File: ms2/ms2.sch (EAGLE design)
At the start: 127 parts, among them J1 POWERPOLE_POWER25A, J10 RS485_1, J11 I2C, J12 TTL_SERIAL, J13 Radio, J14 RS485_3, J2 RAIN, J3 ADC1, J4 ON, J5 D1, J6 D2, J7 ADC2, J8 LED-EN, J9 RS485_2, Q1 DMG6602SVT, Q2 DMG6602SVT, Q3 DMG6602SVT, Q4 DMG6602SVT, U1 LT1934ES6TRMPBF, U2 LT1934ES6TRMPBF, U3 DS3231SN, U4 ISL3179EIBZ, U5 ISL3179EIBZ, U6 ISL3179EIBZ, X1 KUSBVX-BS1N

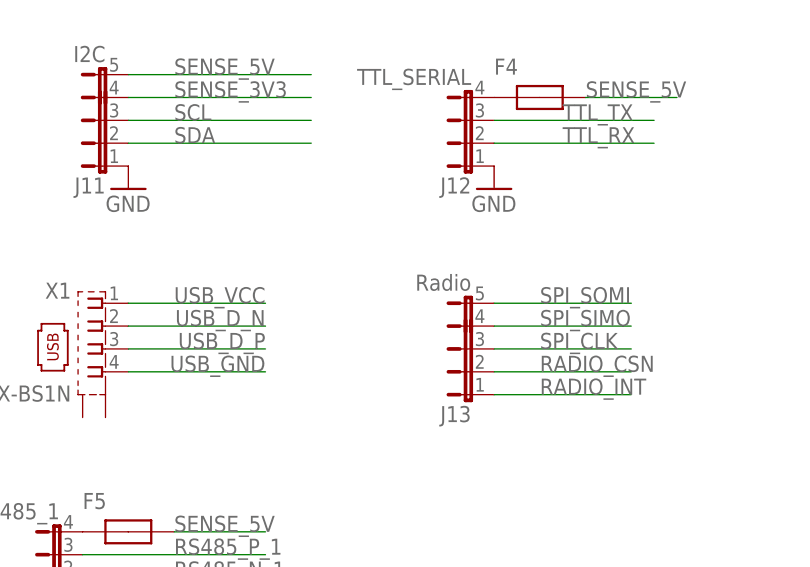
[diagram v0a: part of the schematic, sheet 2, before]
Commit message: CC1120 rotated
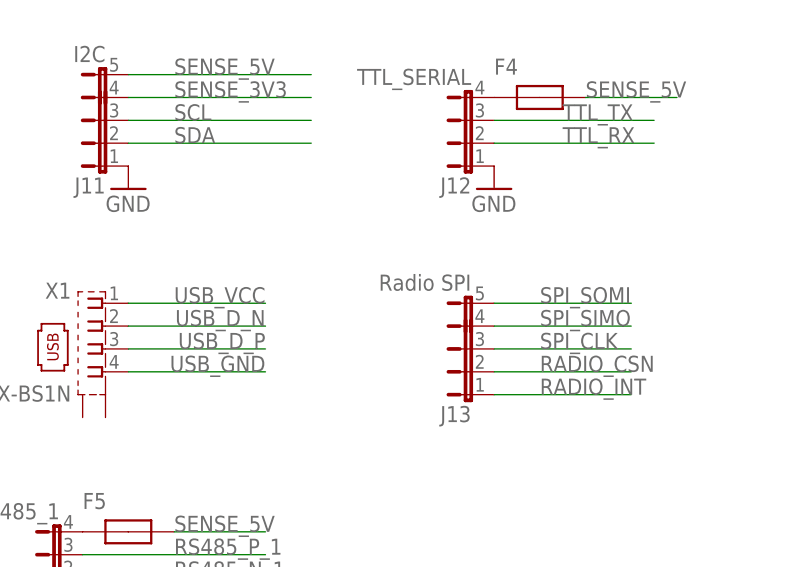
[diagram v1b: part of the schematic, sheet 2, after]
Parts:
- J13: value Radio -> Radio SPI
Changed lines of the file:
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@@
 <?xml version="1.0" encoding="utf-8"?>
 <!DOCTYPE eagle SYSTEM "eagle.dtd">
-<eagle version="6.4">
+<eagle version="6.5.0">
 <drawing>
 <settings>
@@
 <part name="GND10" library="glacsweb" deviceset="GND" device=""/>
 <part name="JP3" library="SparkFun-Passives" deviceset="JUMPER-2" device="SMD-NC"/>
-<part name="J13" library="farnell-parts" deviceset="5-PIN-MOLEX" device="" value="Radio"/>
+<part name="J13" library="farnell-parts" deviceset="5-PIN-MOLEX" device="" value="Radio SPI"/>
 <part name="R16" library="resistor" deviceset="R-EU_" device="R0805" value="56"/>
 <part name="LED3" library="led" deviceset="LED" device="CHIP-LED0805" value="RAIN"/>

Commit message: Work on MS2
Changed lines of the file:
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@@
 <?xml version="1.0" encoding="utf-8"?>
 <!DOCTYPE eagle SYSTEM "eagle.dtd">
-<eagle version="6.5.0">
+<eagle version="6.4">
 <drawing>
 <settings>
@@
 <net name="TXEN" class="0">
 <segment>
+<pinref part="U$5" gate="G$1" pin="CA0"/>
+<wire x1="38.1" y1="177.8" x2="20.32" y2="177.8" width="0.1524" layer="91"/>
+<label x="20.32" y="177.8" size="1.778" layer="95"/>
+</segment>
+<segment>
+<pinref part="U6" gate="A" pin="~RE"/>
+<wire x1="172.72" y1="76.2" x2="170.18" y2="76.2" width="0.1524" layer="91"/>
+<label x="160.02" y="76.2" size="1.778" layer="95"/>
+<pinref part="U6" gate="A" pin="DE"/>
+<wire x1="170.18" y1="76.2" x2="160.02" y2="76.2" width="0.1524" layer="91"/>
+<wire x1="172.72" y1="73.66" x2="170.18" y2="73.66" width="0.1524" layer="91"/>
+<wire x1="170.18" y1="73.66" x2="170.18" y2="76.2" width="0.1524" layer="91"/>
+<junction x="170.18" y="76.2"/>
+<pinref part="U5" gate="A" pin="~RE"/>
+<wire x1="175.26" y1="127" x2="172.72" y2="127" width="0.1524" layer="91"/>
+<label x="160.02" y="127" size="1.778" layer="95"/>
+<pinref part="U5" gate="A" pin="DE"/>
+<wire x1="172.72" y1="127" x2="160.02" y2="127" width="0.1524" layer="91"/>
+<wire x1="175.26" y1="124.46" x2="172.72" y2="124.46" width="0.1524" layer="91"/>
+<wire x1="172.72" y1="124.46" x2="172.72" y2="127" width="0.1524" layer="91"/>
+<junction x="172.72" y="127"/>
+<wire x1="160.02" y1="76.2" x2="160.02" y2="127" width="0.1524" layer="91"/>
 <pinref part="U4" gate="A" pin="~RE"/>
 <wire x1="175.26" y1="175.26" x2="172.72" y2="175.26" width="0.1524" layer="91"/>
@@
 <wire x1="172.72" y1="172.72" x2="172.72" y2="175.26" width="0.1524" layer="91"/>
 <junction x="172.72" y="175.26"/>
-</segment>
-<segment>
-<pinref part="U$5" gate="G$1" pin="CA0"/>
-<wire x1="38.1" y1="177.8" x2="20.32" y2="177.8" width="0.1524" layer="91"/>
-<label x="20.32" y="177.8" size="1.778" layer="95"/>
-</segment>
-<segment>
-<pinref part="U5" gate="A" pin="~RE"/>
-<wire x1="175.26" y1="127" x2="172.72" y2="127" width="0.1524" layer="91"/>
-<label x="160.02" y="127" size="1.778" layer="95"/>
-<pinref part="U5" gate="A" pin="DE"/>
-<wire x1="172.72" y1="127" x2="160.02" y2="127" width="0.1524" layer="91"/>
-<wire x1="175.26" y1="124.46" x2="172.72" y2="124.46" width="0.1524" layer="91"/>
-<wire x1="172.72" y1="124.46" x2="172.72" y2="127" width="0.1524" layer="91"/>
-<junction x="172.72" y="127"/>
-</segment>
-<segment>
-<pinref part="U6" gate="A" pin="~RE"/>
-<wire x1="172.72" y1="76.2" x2="170.18" y2="76.2" width="0.1524" layer="91"/>
-<label x="157.48" y="76.2" size="1.778" layer="95"/>
-<pinref part="U6" gate="A" pin="DE"/>
-<wire x1="170.18" y1="76.2" x2="157.48" y2="76.2" width="0.1524" layer="91"/>
-<wire x1="172.72" y1="73.66" x2="170.18" y2="73.66" width="0.1524" layer="91"/>
-<wire x1="170.18" y1="73.66" x2="170.18" y2="76.2" width="0.1524" layer="91"/>
-<junction x="170.18" y="76.2"/>
-</segment>
-</net>
+<wire x1="160.02" y1="127" x2="160.02" y2="175.26" width="0.1524" layer="91"/>
+<wire x1="160.02" y1="175.26" x2="160.02" y2="198.12" width="0.1524" layer="91"/>
+<wire x1="160.02" y1="198.12" x2="149.86" y2="198.12" width="0.1524" layer="91"/>
+<junction x="160.02" y="175.26"/>
+<junction x="160.02" y="127"/>
+<label x="149.86" y="198.12" size="1.778" layer="95"/>
+</segment>
+</net>

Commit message: Added LTSpice schematic of Switch mode + LDO combo.
Work on MS2.
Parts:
- removed JP3: (no value), SparkFun-Passives:JUMPER-2SMD-NC
- removed L2, L6: 20uH, rcl:L-EU6000-XXX-RC
- added 12V_OUT: POWERPOLE_POWER25A, powerpoles:POWERPOLE_POWER25A
- added 3.4V: TPB2,54, testpad:TPB2,54
- added C23: 0.1uF, resistor:C-EUC0805
- added C24: 100uF, rcl:CPOL-EUE
- added D10, D6, D7, D8, D9: (no value), diode:ZENER-DIODESMB
- added D11, D12: MBR0530T1G, diode:MBR0520LT
- added F10, F11, F12, F13, F14: MCF0805, farnell-parts:MCF0805
- added JP4: PS EN, pinhead:PINHD-1X2
- added JP6: 3.3V Out EN, pinhead:PINHD-1X2
- added Q5: DMG6602SVT, farnell-parts:DMG6602SVT
- added R33, R35: 100K, resistor:R-EU_R0805
- added R34, R36, R37: 1M, resistor:R-EU_R0805
- added U7: TPD2E001IDRLRQ1, Texas Instruments_By_element14_Batch_1:TPD2E001IDRLRQ1
- added U8, U9: TPS79333DBVR, CC11x:TPS79333DBVR
- C16: value 330uF -> 1uF; device rcl:CPOL-EUE5-8.5 -> resistor:C-EUC0805
- C17: value (none) -> 0.1uF
- C18: value (none) -> 2.2uF; device resistor:CPOL-EUB/3528-21R -> resistor:C-EUC0805
- C6: value 330uF -> 2.2uF; device rcl:CPOL-EUE5-8.5 -> resistor:C-EUC0805
- C7: value (none) -> 100uF; device resistor:C-EUC0805 -> rcl:CPOL-EUE
- C8: value (none) -> 1uF; device resistor:CPOL-EUB/3528-21R -> resistor:C-EUC0805
- JP1: device SparkFun-Passives:JUMPER-2SMD-NO -> pinhead:PINHD-1X5
- JP2: value (none) -> 5V Out EN; device SparkFun-Passives:JUMPER-2SMD-NO -> pinhead:PINHD-1X2
- R3: value 604K -> 562K
- R4: value 100K -> 1M
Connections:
- net RADIO_INT renamed RADIO_GPIO0
- net RGND renamed RADIO_GND
- net RS485_N_3 renamed RS4853_N
- net RS485_P_1 renamed RS4851_P
- net RS485_P_2 renamed RS4852_P
- net RS485_P_3 renamed RS4853_P
- net SCL renamed I2C_SCL
- net SDA renamed I2C_SDA
- net SPI_CLK renamed RADIO_SPI_CLK
- net SPI_SIMO renamed RADIO_SPI_MOSI
- net SPI_SOMI renamed RADIO_SPI_MISO
- net TXEN renamed TX_EN
- removed net AGND: AGND.TP, C10.2, J3.3, J7.3, JP5.2, R9.1, U$5.AGND
- removed net DC_IN: D1.A, J4.2, Q1G$2.S, R5.2
- removed net N$107: C4.1, C5.+, D3.A, L1.P$2, L2.1, R2.2
- removed net N$14: 5V.TP, C16.+, C17.1, C18.+, JP2.1, L6.2
- removed net RADIO_CCA_STATUS: U$5.TB3, U$8.GPIO3
- removed net RS485_N_1: J10.2, R30.1, U4.B/Z
- removed net RS485_N_2: J9.2, R27.1, U5.B/Z
- removed net USB_VCC: U$5.USB-5V, X1.1
- removed net VCC_3V3: C19.2, F3.P$2, JP1.1, Q2G$2.S, Q4G$2.S, R13.2, R18.2, R7.2, U$5.D-3V, U$6.VCCB, U3.VCC
- removed net VCC_HP2_SW: C12.1, Q3G$2.D, U2.!SHDN, U2.VIN
- new net +12V: C3.+, D6.C, F11.P$2, JP4.1, VCC.TP
- new net +3V3: C19.2, D8.C, F14.P$2, F3.P$2, JP6.2, Q2G$2.S, Q4G$2.S, R13.2, R18.2, R7.2, U$5.D-3V, U$6.VCCB, U3.VCC
- new net +3V4: 3.4V.TP, C4.1, C5.+, C8.1, D3.A, L1.P$2, R2.2, R36.2, U8.EN, U8.IN
- new net BLUE: JP1.5
- new net GNDA: AGND.TP, C10.2, D10.A, J3.3, J7.3, JP5.2, R9.1, U$5.AGND
- new net GREEN: F14.P$1, JP1.4
- new net N$29: C12.1, D12.C, U2.VIN
- new net N$3: C14.1, C15.+, C16.1, D5.A, L5.2, R20.2, R37.2, U9.EN, U9.IN
- new net N$32: C6.1, C7.+, JP6.1, U8.OUT, VCC_3V.TP
- new net N$34: U$5.TA1
- new net N$35: U$5.TA2
- new net N$36: U$5.ADC6
- new net N$37: U$5.ADC3
- new net N$38: U$5.ADC4
- new net N$39: U$5.ADC0
- new net N$40: U$5.ADC_3V3
- new net N$41: U$5.USER_INT
- new net N$42: U$5.ALERT
- new net N$43: Q5G$1.D@1, Q5G$2.G, R12.1
- new net N$44: F10.P$2, Q5G$2.S, R12.2
- new net N$45: C1.1, D11.C, U1.VIN
- new net N$46: R33.1, U1.!SHDN
- new net N$47: D11.A, JP4.2, Q3G$2.S, R11.2, R33.2, R4.2
- new net N$48: R35.1, U2.!SHDN
- new net N$49: D12.A, Q3G$2.D, R34.2, R35.2
- new net N$5: D1.C, F11.P$1
- new net N$54: C17.1, U9.NR
- new net RADIO_GPIO2: U$5.TB3, U$8.GPIO2
- new net RED: F12.P$1, JP1.1
- new net RS4852_N: J10.2, J9.2, R27.1, R30.1, U4.B/Z, U5.B/Z
- new net SENSE_12V: 12V_OUT.V+, D9.C, F12.P$2, Q5G$2.D
- new net USB_5V: U$5.USB-5V, U7.VCC, X1.1
- new net YELLOW: F13.P$1, JP1.3
- net ADC_7: now also D10.C
- net BATV_EN: no longer JP3.2, Q1G$1.G, R4.2
- net GND: now also 12V_OUT.GND, C16.2, C18.2, C23.2, C24.-, C6.2, C7.-, C8.2, D6.A, D7.A, D8.A, D9.A, JP1.2, Q5G$1.S, R34.1, R36.1, R37.1, U8.GND, U9.GND; no longer C16.-, C18.-, C6.-, C7.2, C8.-, R12.1
- net N$13: now also 5V.TP, C18.1, C24.+, JP2.2, U9.OUT; no longer C6.+, C7.1, C8.+, JP1.2, L2.2, VCC_3V.TP
- net N$6: now also C23.1, U8.NR; no longer C14.1, C15.+, D5.A, L5.2, L6.1, R20.2
- net SENSE_5V: now also D7.C, F13.P$2, JP2.1; no longer JP2.2
- net SENSE_EN: now also Q1G$1.G, Q5G$1.G; no longer JP3.1, R12.2
- net TTL_TX: now also U$6.A8
- net USB_D_N: now also U7.IO1
- net USB_D_P: now also U7.IO2
- net USB_GND: now also U7.GND
- net VCC: now also D1.A, F10.P$1, J4.2, Q1G$2.S, R5.2; no longer C1.1, C3.+, D1.C, Q3G$2.S, R11.2, U1.!SHDN, U1.VIN, VCC.TP
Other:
- note added: "12V Sense EN"
- note added: "12V input"
- note added: "Alternative power supply"
- note added: "Analogue Inputs"
- note added: "Place C8 as close to U8 as possible. Place C6 as close to U8 as possible. Ensure that U8 has a good thermal plane. Power supply section should have its own GND planes with only two connections to GND."
- note added: "RS485 Drivers"
- note added: "Radio Power"
- note added: "Re-design as per datasheet: http://www.farnell.com/datasheets/1712353.pdf"
- note added: "Sensor Power"
- note removed: "Analog Inputs"
- note removed: "BatV / Sense Link"
- note removed: "DC IN"
- note removed: "RS485 Driver"

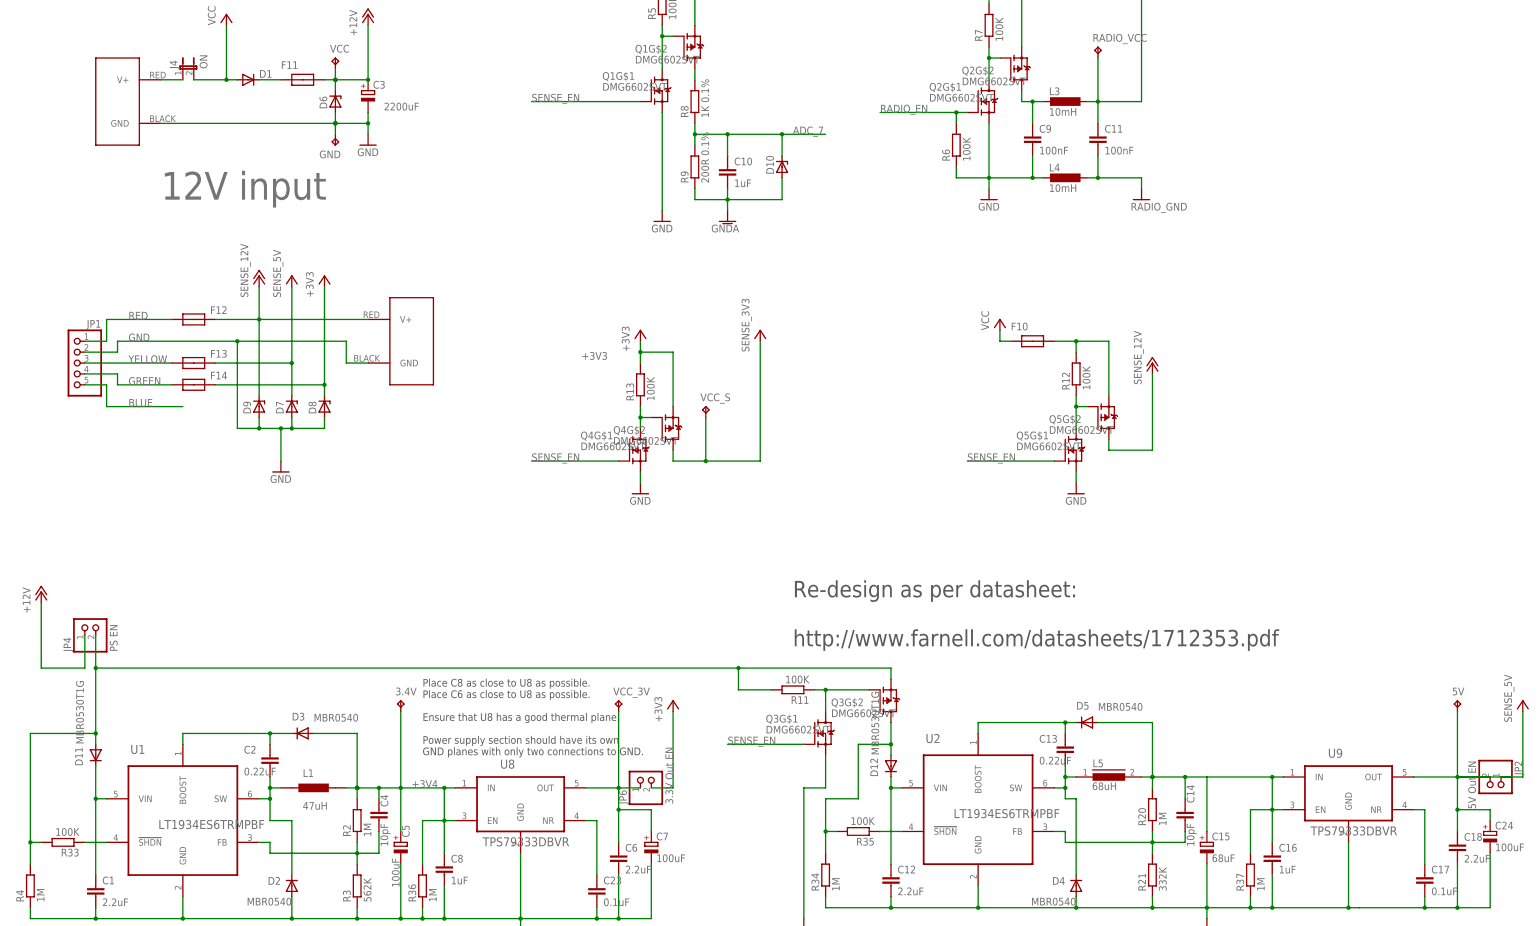
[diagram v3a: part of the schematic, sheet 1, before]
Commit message: "new" power supply implemented on ms2
Added Eagle files for CC1120 breakout.
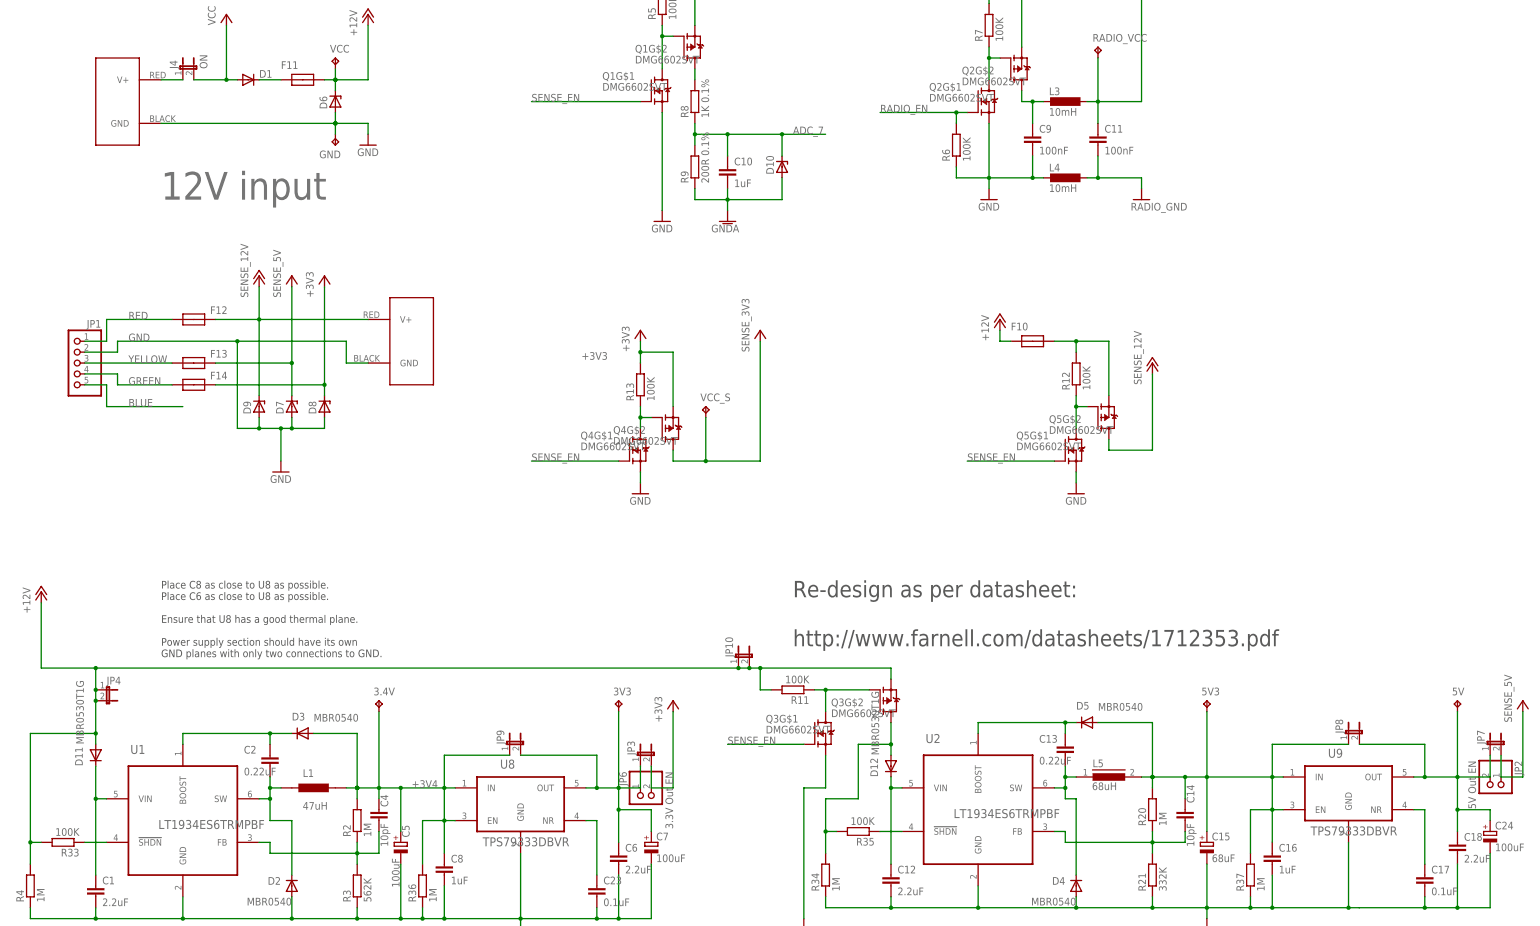
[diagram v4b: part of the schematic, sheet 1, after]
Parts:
- removed C3: 2200uF, rcl:CPOL-EUE5-13
- added 5V3: 5V B, testpad:TPB2,54
- added JP10, JP3, JP7, JP8, JP9: (no value), SparkFun-Passives:JUMPER-2SMD-NO
- JP4: value PS EN -> (none); device pinhead:PINHD-1X2 -> SparkFun-Passives:JUMPER-2SMD-NO
- renumbered VCC_3V to 3V3
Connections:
- removed net N$47: D11.A, JP4.2, Q3G$2.S, R11.2, R33.2, R4.2
- new net 5V3: 5V3.TP, C14.1, C15.+, C16.1, D5.A, JP8.1, L5.2, R20.2, R37.2, U9.EN, U9.IN
- new net N$14: U3.~INT/SQW
- new net N$52: U3.~RST
- net +12V: now also D11.A, F10.P$1, JP10.1, JP10.2, JP4.2, Q3G$2.S, R11.2, R33.2, R4.2; no longer C3.+
- net +3V3: now also JP3.2
- net +3V4: now also JP9.1
- net GND: no longer C3.-
- net N$13: now also JP7.1, JP8.2
- net N$3: now also U3.32KHZ; no longer C14.1, C15.+, C16.1, D5.A, L5.2, R20.2, R37.2, U9.EN, U9.IN
- net N$32: now also JP3.1, JP9.2
- net SENSE_5V: now also JP7.2
- net VCC: no longer F10.P$1
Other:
- moved on the sheet: 3.4V, JP6

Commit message: More MS2 layout work.
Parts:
- removed D10: (no value), diode:ZENER-DIODESMB
- removed JP1: (no value), pinhead:PINHD-1X5
- added H1: JST-S06B-PASK-2, CC11x:JST-S06B-PASK-2
- added R38: 1M, resistor:R-EU_R0805
- F12: value MCF0805 -> 250mA
- JP5: value GND-LINK -> LINK
- LED10: value BAT_EN -> RADIO_EN
- X1: value KUSBVX-BS1N -> 67068-9000; device con-kycon:KUSBVX-BS1N -> con-usb-3:USB-B-H
- renumbered U$6 to U10
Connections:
- removed net 485_3V3: C20.1, C21.1, C22.1, U4.VCC, U5.VCC, U6.VCC
- removed net BATV_EN: R25.2
- removed net BLUE: JP1.5
- removed net GREEN: F14.P$1, JP1.4
- removed net N$50: LED10.A, R25.1
- removed net RED: F12.P$1, JP1.1
- removed net YELLOW: F13.P$1, JP1.3
- new net ALT_3V3: F12.P$1, H1.2
- new net ALT_5V: F13.P$1, H1.3
- new net ALT_9V: F14.P$1, H1.4
- new net RS4851_N: J10.2, R30.1, U4.B/Z
- net +3V3: now also F12.P$2; no longer D8.C, F14.P$2
- net 485_RX_1: now also U10.A2; no longer U10.A1
- net 485_RX_2: now also U10.A3; no longer U10.A2
- net 485_RX_3: now also U10.A4; no longer U10.A3
- net 485_TX_1: now also U10.A6; no longer U10.A5
- net 485_TX_2: now also U10.A7; no longer U10.A6
- net 485_TX_3: now also U10.A8; no longer U10.A7
- net ADC_7: no longer D10.C
- net GND: now also H1.1, H1.5, R38.2; no longer D7.A, D8.A, D9.A, JP1.2
- net GNDA: no longer D10.A
- net LGND: no longer LED10.C
- net RS4852_N: no longer J10.2, R30.1, U4.B/Z
- net SENSE_12V: now also F14.P$2, R17.2; no longer D9.C, F12.P$2
- net SENSE_3V3: now also C20.1, C21.1, C22.1, R38.1, U4.VCC, U5.VCC, U6.VCC
- net SENSE_5V: no longer D7.C
- net SENSE_EN: now also H1.6
- net TTL_RX: now also U10.A1; no longer U10.A4
- net TTL_TX: now also U10.A5; no longer U10.A8
- net USB_5V: now also X1.VBUS; no longer X1.1
- net USB_D_N: now also X1.D-; no longer X1.2
- net USB_D_P: now also X1.D+; no longer X1.3
- net USB_GND: now also X1.GND; no longer X1.4
- net VCC: no longer R17.2
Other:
- note added: "200mA"
- note added: "250mA"
- note added: "500mA"
- note added: "MOLEX 67068-9000 Onecall 1463094"
- moved on the sheet: AGND, D7, D8, D9, F10, F12, F13, F14, J8, JP5, LED1, LED10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

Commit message: MS2 as submitted for manufacture
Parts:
- removed BATV_B: 5V B, testpad:TPB2,54
- removed D6, D7, D8, D9: (no value), diode:ZENER-DIODESMB
- removed F12: 250mA, farnell-parts:MCF0805
- removed F13, F14: MCF0805, farnell-parts:MCF0805
- added F15, F16: MCF0805, farnell-parts:MCF0805
- added JP1: SENSE_EN, pinhead:PINHD-1X2
- added JP11: RADIO_EN, pinhead:PINHD-1X2
- added JP12: (no value), SparkFun-Passives:JUMPER-2SMD-NO
- added R39: 100K, resistor:R-EU_R0805
- added U11: SN74HC21PW, CC11x:SN74HC21PW
- 12V_OUT, J1: value POWERPOLE_POWER25A -> POWERPOLE_POWER45A; device powerpoles:POWERPOLE_POWER25A -> powerpoles:POWERPOLE_POWER45A
- LED10: value RADIO_EN -> VCC
- R25: value 56 -> 560
- R28: value 47K -> 100K
- R38: value 1M -> 100K
- renumbered U$5 to Z1, VCC to 12V
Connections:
- removed net ALT_3V3: F12.P$1, H1.2
- removed net ALT_5V: F13.P$1, H1.3
- removed net ALT_9V: F14.P$1, H1.4
- new net N$47: F16.P$1, J11.4
- new net N$50: F15.P$1, J11.6
- new net N$53: LED10.A, R25.1
- new net N$57: U10.B3
- new net N$58: U10.B4
- new net TX_EN_BUFF: U10.A2, U4.DE, U4.~RE, U5.DE, U5.~RE, U6.DE, U6.~RE
- new net UART1_RX_BUFF: JP12.2, U10.A1, U11.2Y
- net +12V: no longer D6.C
- net +3V3: now also H1.2, JP1.1, JP11.1; no longer F12.P$2
- net 485_RX_1: now also JP12.1, U11.2B; no longer U10.A2
- net 485_RX_2: now also R28.1, U11.2C; no longer U10.A3
- net 485_RX_3: now also R38.1, U11.2D; no longer U10.A4
- net GND: now also U11.1A, U11.1B, U11.1C, U11.1D, U11.GND, Z1.CPDGND; no longer D6.A, R38.2
- net LGND: now also LED10.C
- net N$8: now also U11.1Y; no longer R28.1, U10.OE
- net RADIO_EN: now also JP11.2
- net SENSE_12V: now also H1.4; no longer F14.P$2
- net SENSE_3V3: now also F16.P$2, R38.2, R39.2, U10.A3, U10.A4, U11.VCC; no longer J11.4, R38.1
- net SENSE_5V: now also F15.P$2, H1.3; no longer F13.P$2, J11.6
- net SENSE_EN: now also JP1.2, U10.OE
- net TTL_RX: now also R39.1, U11.2A; no longer U10.A1
- net TX_EN: now also U10.B2; no longer U4.DE, U4.~RE, U5.DE, U5.~RE, U6.DE, U6.~RE
- net UART1_RX: no longer U10.B2, U10.B3, U10.B4
- net VBAT_B: no longer BATV_B.TP
- net VCC: now also R25.2
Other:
- note added: "Test Jumpers"
- note removed: "250mA"
- moved on the sheet: F4, J12, J13, LED10, R25, R28, R31
